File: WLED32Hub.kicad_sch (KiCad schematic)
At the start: 76 parts, among them J1 USB_C_Receptacle_PowerOnly_6P, J10 WAGO, J11 WAGO, J12 WAGO, J13 WAGO, J14 WAGO, J15 WAGO, J16 WAGO, J17 WAGO, J18 WAGO, J19 Conn_01x05, J2 Power WAGO, J3 WAGO, J4 WAGO, J5 WAGO, J6 WAGO, J7 WAGO, J8 WAGO, J9 WAGO, Q1 IRLB8721PBF, Q10 IRLB8721PBF, Q11 IRLB8721PBF, Q12 IRLB8721PBF, Q13 IRLB8721PBF, Q14 IRLB8721PBF, Q15 IRLB8721PBF, Q16 IRLB8721PBF, Q2 IRLB8721PBF, Q3 IRLB8721PBF, Q4 IRLB8721PBF, Q5 IRLB8721PBF, Q6 IRLB8721PBF, Q7 IRLB8721PBF, Q8 IRLB8721PBF, Q9 IRLB8721PBF, U1 ESP32-DevKit-V3.0, U2 Arduino-Pro-Micro

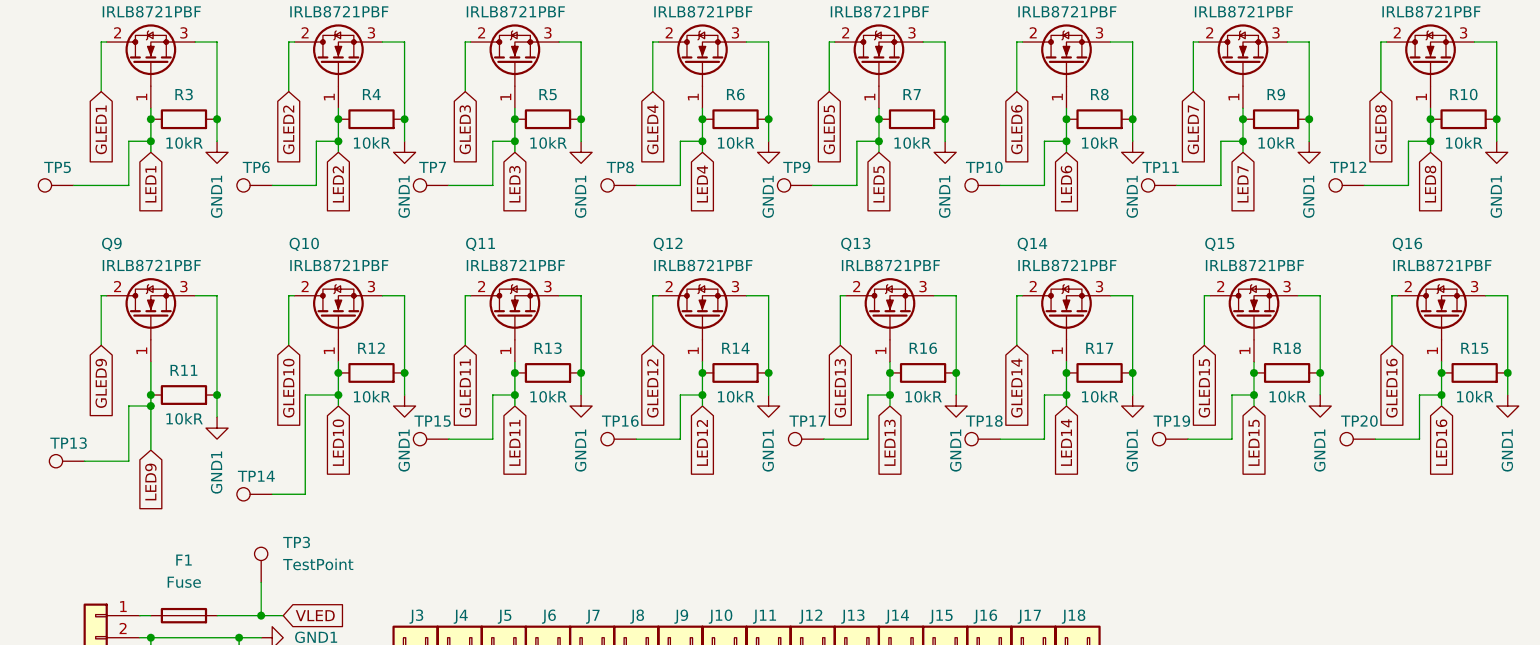
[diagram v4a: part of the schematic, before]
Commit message: Silkscreen Markers + Test Point Connections
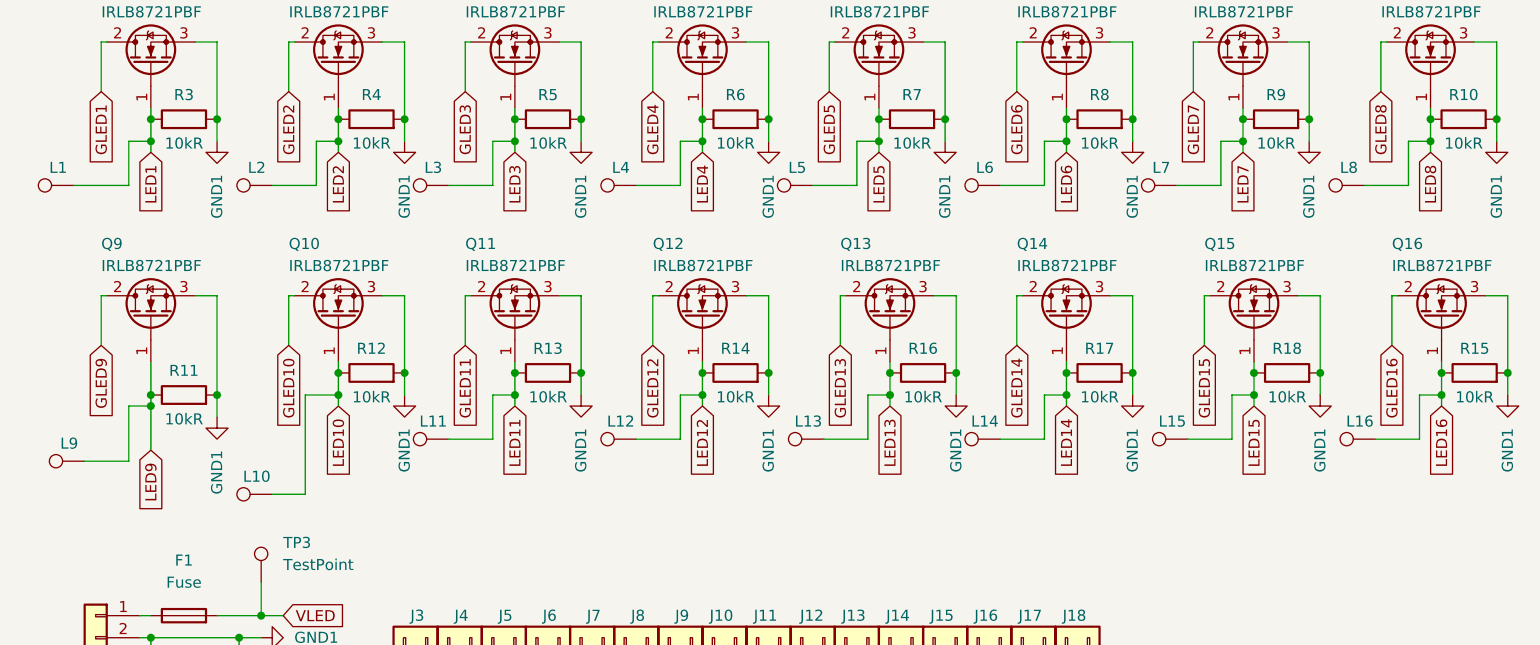
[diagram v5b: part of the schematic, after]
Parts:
- renumbered TP5 to L1, TP14 to L10, TP15 to L11, TP16 to L12, TP17 to L13, TP18 to L14, TP19 to L15, TP20 to L16, TP6 to L2, TP7 to L3, TP8 to L4, TP9 to L5, TP10 to L6, TP11 to L7, TP12 to L8, TP13 to L9
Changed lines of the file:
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@@
 		(on_board yes)
 		(dnp no)
-		(property "Reference" "TP5"
+		(property "Reference" "L1"
 			(at 18.542 102.108 90)
 			(effects
@@
 			(project "WLED32Hub"
 				(path "/b70a5dae-17dd-4b3a-9018-d3dd2220f450"
-					(reference "TP5")
+					(reference "L1")
 					(unit 1)
 				)
@@
 		(on_board yes)
 		(dnp no)
-		(property "Reference" "TP9"
+		(property "Reference" "L5"
 			(at 103.632 102.108 90)
 			(effects
@@
 			(project "WLED32Hub"
 				(path "/b70a5dae-17dd-4b3a-9018-d3dd2220f450"
-					(reference "TP9")
+					(reference "L5")
 					(unit 1)
 				)
@@
 		(on_board yes)
 		(dnp no)
-		(property "Reference" "TP17"
+		(property "Reference" "L13"
 			(at 104.902 131.318 90)
 			(effects
@@
 			(project "WLED32Hub"
 				(path "/b70a5dae-17dd-4b3a-9018-d3dd2220f450"
-					(reference "TP17")
+					(reference "L13")
 					(unit 1)
 				)
@@
 		(on_board yes)
 		(dnp no)
-		(property "Reference" "TP19"
+		(property "Reference" "L15"
 			(at 146.812 131.318 90)
 			(effects
@@
 			(project "WLED32Hub"
 				(path "/b70a5dae-17dd-4b3a-9018-d3dd2220f450"
-					(reference "TP19")
+					(reference "L15")
 					(unit 1)
 				)
@@
 		(on_board yes)
 		(dnp no)
-		(property "Reference" "TP16"
+		(property "Reference" "L12"
 			(at 83.312 131.318 90)
 			(effects
@@
 			(project "WLED32Hub"
 				(path "/b70a5dae-17dd-4b3a-9018-d3dd2220f450"
-					(reference "TP16")
+					(reference "L12")
 					(unit 1)
 				)
@@
 		(on_board yes)
 		(dnp no)
-		(property "Reference" "TP13"
+		(property "Reference" "L9"
 			(at 19.812 133.858 90)
 			(effects
@@
 			(project "WLED32Hub"
 				(path "/b70a5dae-17dd-4b3a-9018-d3dd2220f450"
-					(reference "TP13")
+					(reference "L9")
 					(unit 1)
 				)
@@
 		(on_board yes)
 		(dnp no)
-		(property "Reference" "TP7"
+		(property "Reference" "L3"
 			(at 61.722 102.108 90)
 			(effects
@@
 			(project "WLED32Hub"
 				(path "/b70a5dae-17dd-4b3a-9018-d3dd2220f450"
-					(reference "TP7")
+					(reference "L3")
 					(unit 1)
 				)
@@
 		(on_board yes)
 		(dnp no)
-		(property "Reference" "TP10"
+		(property "Reference" "L6"
 			(at 125.222 102.108 90)
 			(effects
@@
 			(project "WLED32Hub"
 				(path "/b70a5dae-17dd-4b3a-9018-d3dd2220f450"
-					(reference "TP10")
+					(reference "L6")
 					(unit 1)
 				)
@@
 		(on_board yes)
 		(dnp no)
-		(property "Reference" "TP20"
+		(property "Reference" "L16"
 			(at 168.402 131.318 90)
 			(effects
@@
 			(project "WLED32Hub"
 				(path "/b70a5dae-17dd-4b3a-9018-d3dd2220f450"
-					(reference "TP20")
+					(reference "L16")
 					(unit 1)
 				)
@@
 		(on_board yes)
 		(dnp no)
-		(property "Reference" "TP14"
+		(property "Reference" "L10"
 			(at 41.402 137.668 90)
 			(effects
@@
 			(project "WLED32Hub"
 				(path "/b70a5dae-17dd-4b3a-9018-d3dd2220f450"
-					(reference "TP14")
+					(reference "L10")
 					(unit 1)
 				)
@@
 		(on_board yes)
 		(dnp no)
-		(property "Reference" "TP18"
+		(property "Reference" "L14"
 			(at 125.222 131.318 90)
 			(effects
@@
 			(project "WLED32Hub"
 				(path "/b70a5dae-17dd-4b3a-9018-d3dd2220f450"
-					(reference "TP18")
+					(reference "L14")
 					(unit 1)
 				)
@@
 		(on_board yes)
 		(dnp no)
-		(property "Reference" "TP11"
+		(property "Reference" "L7"
 			(at 145.542 102.108 90)
 			(effects
@@
 			(project "WLED32Hub"
 				(path "/b70a5dae-17dd-4b3a-9018-d3dd2220f450"
-					(reference "TP11")
+					(reference "L7")
 					(unit 1)
 				)
@@
 		(on_board yes)
 		(dnp no)
-		(property "Reference" "TP12"
+		(property "Reference" "L8"
 			(at 167.132 102.108 90)
 			(effects
@@
 			(project "WLED32Hub"
 				(path "/b70a5dae-17dd-4b3a-9018-d3dd2220f450"
-					(reference "TP12")
+					(reference "L8")
 					(unit 1)
 				)
@@
 		(on_board yes)
 		(dnp no)
-		(property "Reference" "TP6"
+		(property "Reference" "L2"
 			(at 41.402 102.108 90)
 			(effects
@@
 			(project "WLED32Hub"
 				(path "/b70a5dae-17dd-4b3a-9018-d3dd2220f450"
-					(reference "TP6")
+					(reference "L2")
 					(unit 1)
 				)
@@
 		(on_board yes)
 		(dnp no)
-		(property "Reference" "TP15"
+		(property "Reference" "L11"
 			(at 61.722 131.318 90)
 			(effects
@@
 			(project "WLED32Hub"
 				(path "/b70a5dae-17dd-4b3a-9018-d3dd2220f450"
-					(reference "TP15")
+					(reference "L11")
 					(unit 1)
 				)
@@
 		(on_board yes)
 		(dnp no)
-		(property "Reference" "TP8"
+		(property "Reference" "L4"
 			(at 83.312 102.108 90)
 			(effects
@@
 			(project "WLED32Hub"
 				(path "/b70a5dae-17dd-4b3a-9018-d3dd2220f450"
-					(reference "TP8")
+					(reference "L4")
 					(unit 1)
 				)
